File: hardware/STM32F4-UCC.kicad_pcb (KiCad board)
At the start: 2 copper layers, 111.1 x 61.2 mm, 121 parts, among them J1 DB15, J2 STM32F4_Discovery_Header, J3 RJ45-TRANSFO_W, Q1 IRLML6402, SW1 PE4, SW2 PE5, SW3 PE6, SW4 PE2, U1 RGB, U2 FT230X, U3 DP83848C, U4 MCP1825S-3302E, U5 microSD, X1 50Mhz

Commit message: Ultimos cambios realizados antes de enviar la placa.
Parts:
- C22, C23, C6: footprint Capacitors_ThroughHole:Capacitor5x11RM2.5 -> w_Connectors:Capacitor5x11RM2.5
- J3: footprint RJ45 -> w_Connectors:RJ45
- JP1: footprint Pin_Headers:Pin_Header_Straight_1x03 -> w_Connectors:Pin_Header_Straight_1x03
- JP2, JP3: footprint Pin_Headers:Pin_Header_Straight_1x02 -> w_Connectors:Pin_Header_Straight_1x02
- SW1, SW2, SW3, SW4: footprint w_switch:PCB_PUSH -> w_Connectors:PCB_PUSH
- U1: footprint PLCC4 -> w_Connectors:PLCC4
- U3: footprint lqfp48 -> w_Connectors:lqfp48
- X1: footprint crystal_fa128 -> w_Connectors:crystal_fa128

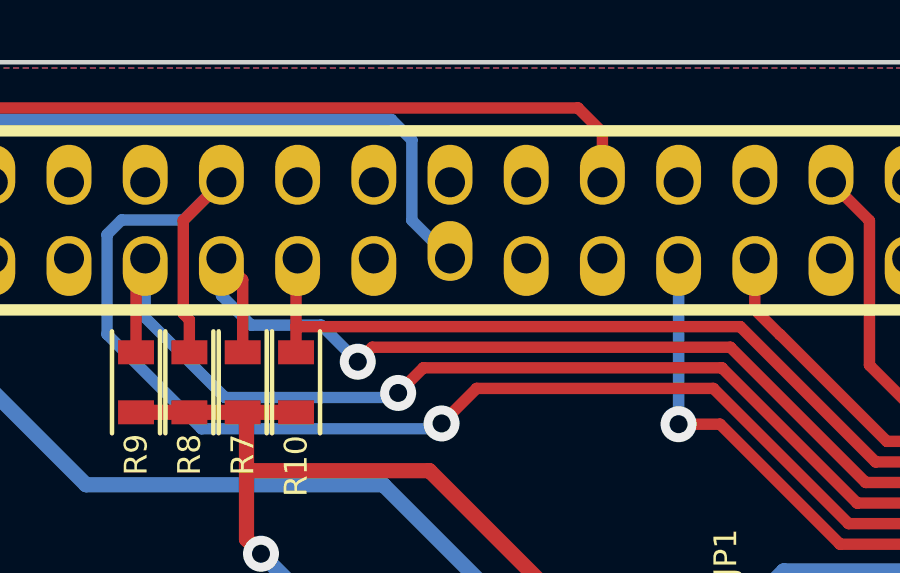
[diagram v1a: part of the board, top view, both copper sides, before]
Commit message: Se acomodaron los archivos para que quede mas prolijo
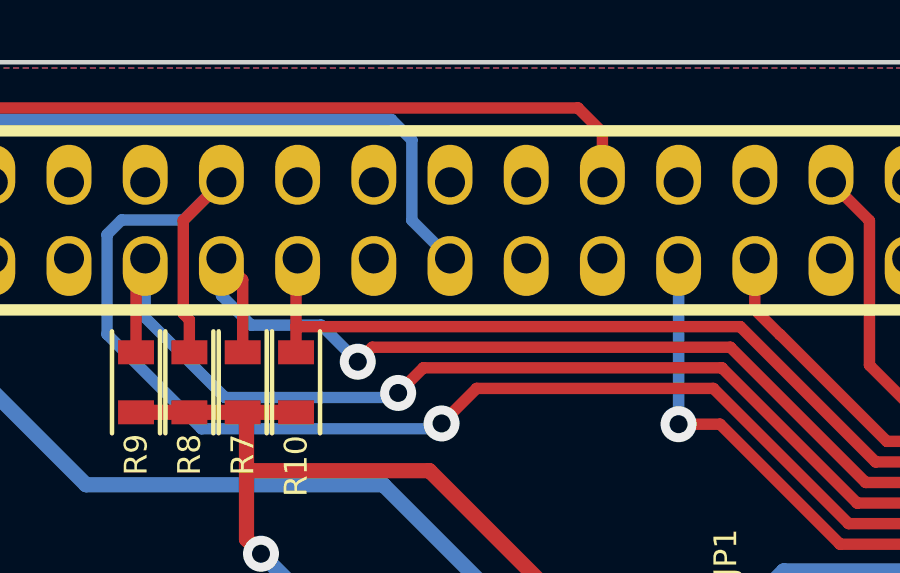
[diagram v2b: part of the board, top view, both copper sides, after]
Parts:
- J2: footprint w_Connectors:stm32f4_discovery_header -> stm32f4_discovery_header
